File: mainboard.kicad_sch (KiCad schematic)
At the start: 0 parts

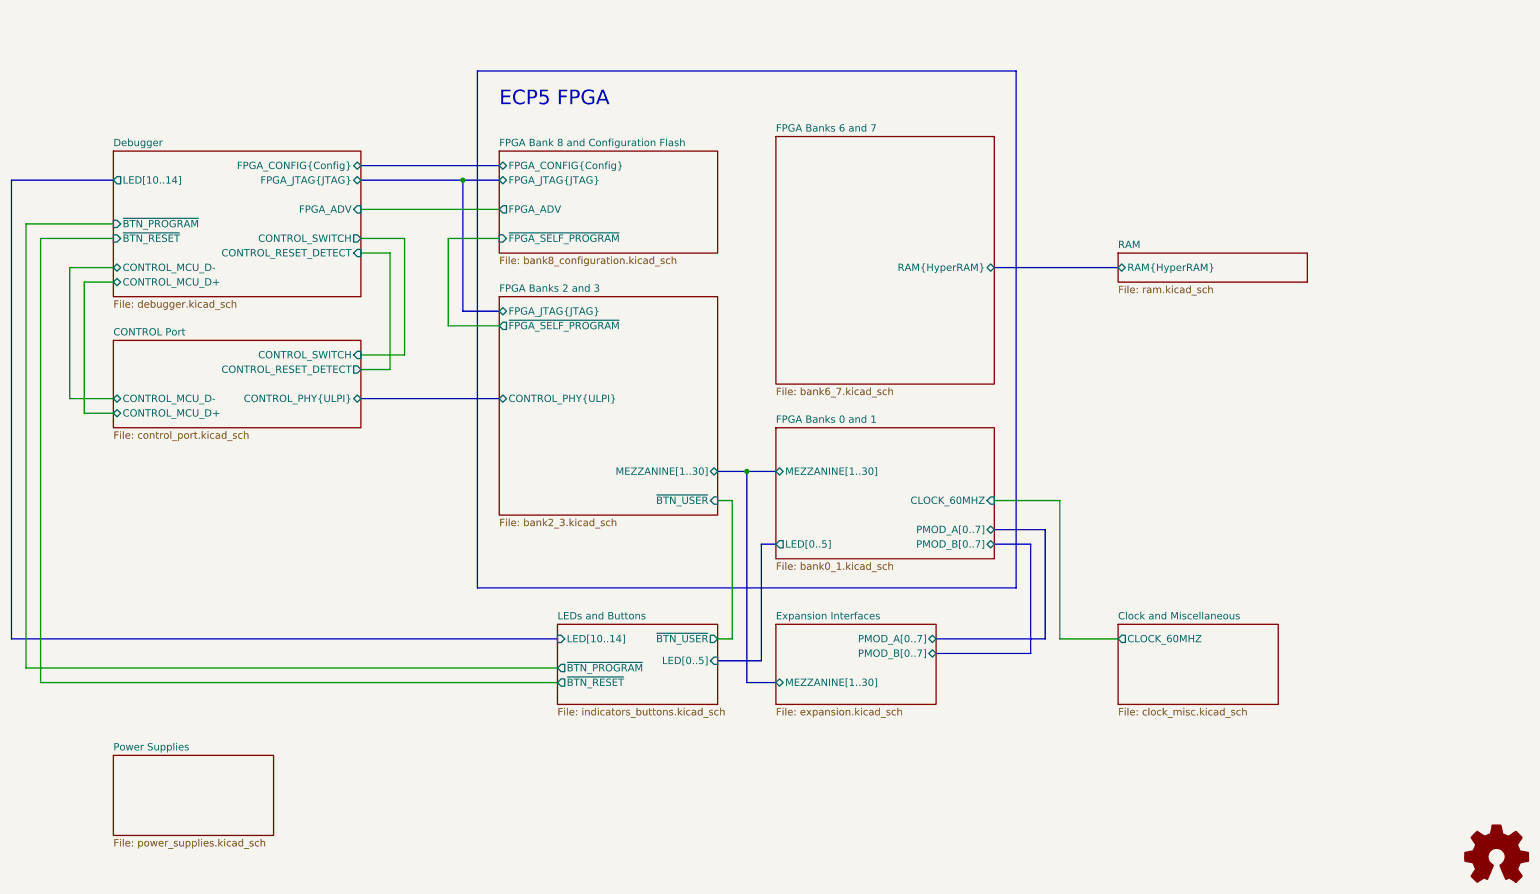
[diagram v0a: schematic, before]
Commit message: Add radio transceiver
Remove Cynthion-specific features
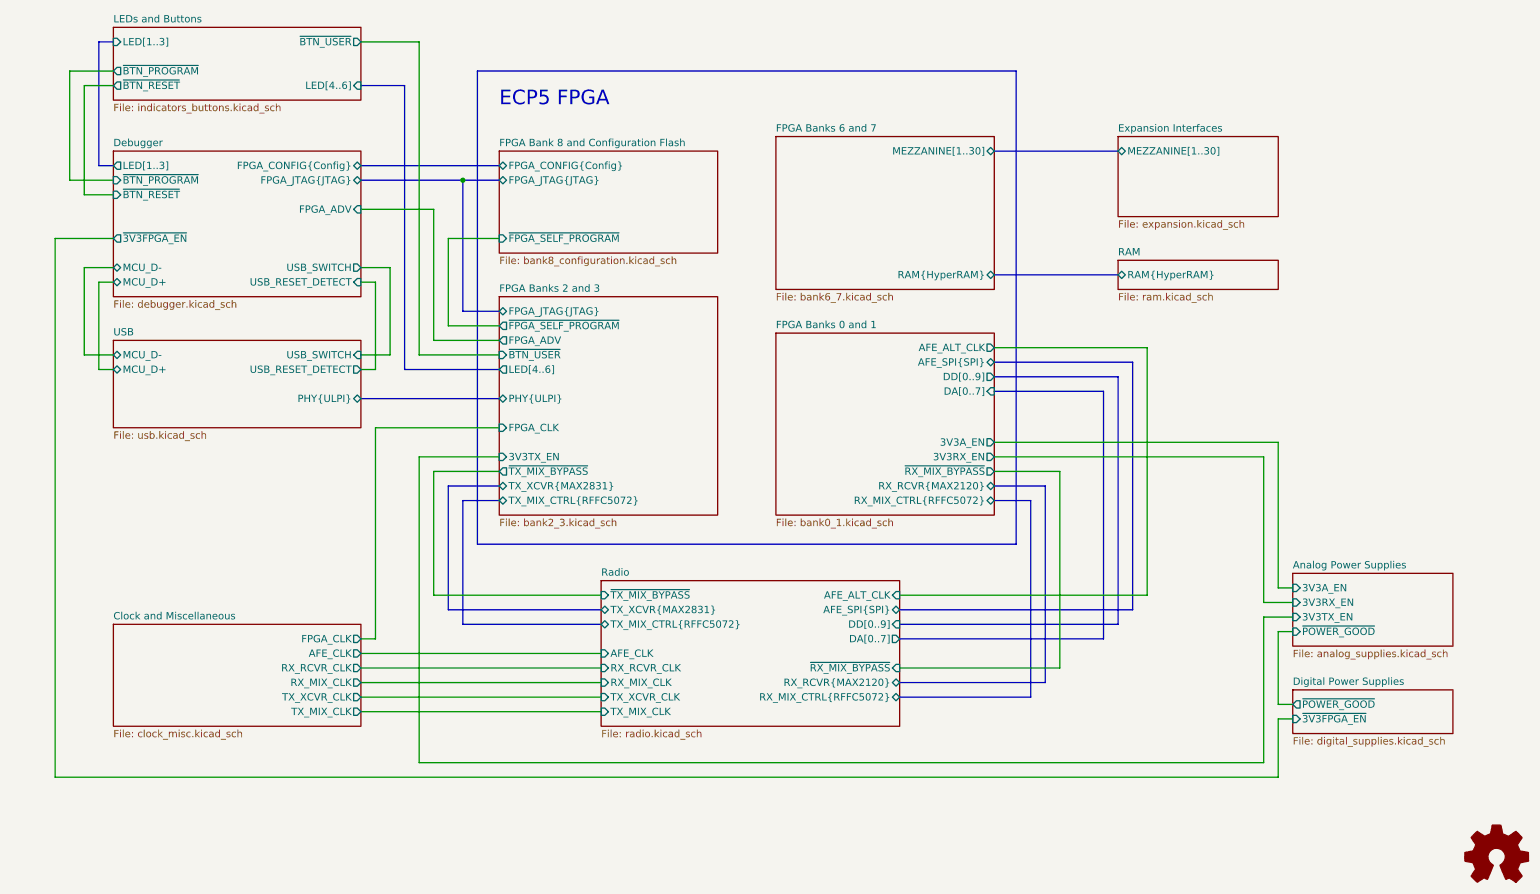
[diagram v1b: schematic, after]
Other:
- sheet CONTROL Port renamed USB
- sheet Power Supplies renamed Digital Power Supplies
- added sheet Analog Power Supplies (analog_supplies.kicad_sch)
- added sheet Radio (radio.kicad_sch)
- sheet Clock and Miscellaneous ports: added AFE_CLK, FPGA_CLK, RX_MIX_CLK, RX_RCVR_CLK, TX_MIX_CLK, TX_XCVR_CLK; removed CLOCK_60MHZ
- sheet Debugger ports: added LED[1..3], MCU_D+, MCU_D-, USB_RESET_DETECT, USB_SWITCH, ~{3V3FPGA_EN}; removed CONTROL_MCU_D+, CONTROL_MCU_D-, CONTROL_RESET_DETECT, CONTROL_SWITCH, LED[10..14]
- sheet Digital Power Supplies: file power_supplies.kicad_sch -> digital_supplies.kicad_sch
- sheet Digital Power Supplies ports: added ~{3V3FPGA_EN}, ~{POWER_GOOD}; removed none
- sheet Expansion Interfaces ports: added none; removed PMOD_A[0..7], PMOD_B[0..7]
- sheet FPGA Bank 8 and Configuration Flash ports: added none; removed FPGA_ADV
- sheet FPGA Banks 0 and 1 ports: added 3V3A_EN, 3V3RX_EN, AFE_ALT_CLK, AFE_SPI{SPI}, DA[0..7], DD[0..9], RX_MIX_CTRL{RFFC5072}, RX_RCVR{MAX2120}, ~{RX_MIX_BYPASS}; removed CLOCK_60MHZ, LED[0..5], MEZZANINE[1..30], PMOD_A[0..7], PMOD_B[0..7]
- sheet FPGA Banks 2 and 3 ports: added 3V3TX_EN, FPGA_ADV, FPGA_CLK, LED[4..6], PHY{ULPI}, TX_MIX_CTRL{RFFC5072}, TX_XCVR{MAX2831}, ~{TX_MIX_BYPASS}; removed CONTROL_PHY{ULPI}, MEZZANINE[1..30]
- sheet FPGA Banks 6 and 7 ports: added MEZZANINE[1..30]; removed none
- sheet LEDs and Buttons ports: added LED[1..3], LED[4..6]; removed LED[0..5], LED[10..14]
- sheet USB: file control_port.kicad_sch -> usb.kicad_sch
- sheet USB ports: added MCU_D+, MCU_D-, PHY{ULPI}, USB_RESET_DETECT, USB_SWITCH; removed CONTROL_MCU_D+, CONTROL_MCU_D-, CONTROL_PHY{ULPI}, CONTROL_RESET_DETECT, CONTROL_SWITCH
- company: Copyright 2023 Great Scott Gadgets -> ${COPYRIGHT}
- title: URTI Mainboard -> ${TITLE}
